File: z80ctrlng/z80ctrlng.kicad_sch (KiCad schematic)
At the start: 43 parts, among them J1 BUS, J2 Micro_SD_Card_Det2, J3 UEXT, J4 SERIAL, J5 Conn_01x04_Pin, Q4 BSS138, SW1 RESET, SW2 SW_DPDT_x2, SW3 SW_SP3T, SW4 SW_DIP_x06, SW5 SW_DPDT_x2, SW6 SW_DPDT_x2, U1 AVR128DB64x-xPT, U2 MIC5504-3.3YM5, U3 MCP7940N-xST, U5 74HCT574, U6 74HCT257, U7 AS6C4008-55PCN, Y1 32kHz

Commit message: Finishing up...
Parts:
- removed J5: Conn_01x04_Pin, Connector_PinHeader_2.54mm:PinHeader_1x04_P2.54mm_Horizontal, symbol Connector:Conn_01x04_Pin
- removed SW5, SW6: SW_DPDT_x2, SamacSys_Parts:JS202011CQN, symbol Switch:SW_DPDT_x2
- added C15: 0.1uf, Capacitor_SMD:C_0402_1005Metric, symbol Device:C_Small
- added D1: LED, LED_SMD:LED_0805_2012Metric, symbol Device:LED
- added J6: UPDI, Connector_PinHeader_2.54mm:PinHeader_1x04_P2.54mm_Horizontal, symbol Connector_Generic:Conn_01x04
- added R10: 330, Resistor_SMD:R_0402_1005Metric, symbol Device:R_Small
- added SW5, SW6: SW_DPST, SamacSys_Parts:JS202011CQN, symbol Switch:SW_DPST
- BT1: footprint Battery:BatteryHolder_Keystone_3000_1x12mm -> Battery:BatteryHolder_Keystone_3001_1x12mm
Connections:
- net +3.3V: now also D1.2 (A)
- net +5V: now also C15.1, J6.3 (Pin_3)
- net GND: now also C15.2, J6.2 (Pin_2)
- net SCL: now also SW6.2
- net SCL3V: now also SW6.1
- net SCL5V: now also SW5.1
- net SDA: now also SW6.5
- net SDA3V: now also SW6.4
- net SDA5V: now also SW5.4
- net USER6: now also SW5.2
- net USER7: now also SW5.5
- net ~{RESET}: now also J6.1 (Pin_1)
- net ~{SDCS}: now also R10.1
- net at J3.10 (Pin_10), SW3.2: now also SW3.5
- net UPDI: now reaches U1.51 (UPDI)
- net UPDI: now also J6.4 (Pin_4)
- new net: D1.1 (K), R10.2
- no-connect marks 14 -> 11
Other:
- company: (none) -> (C) 2023 J.B. Langston
- title: (none) -> z80ctrl NG
- moved on the sheet: R9, SW2B

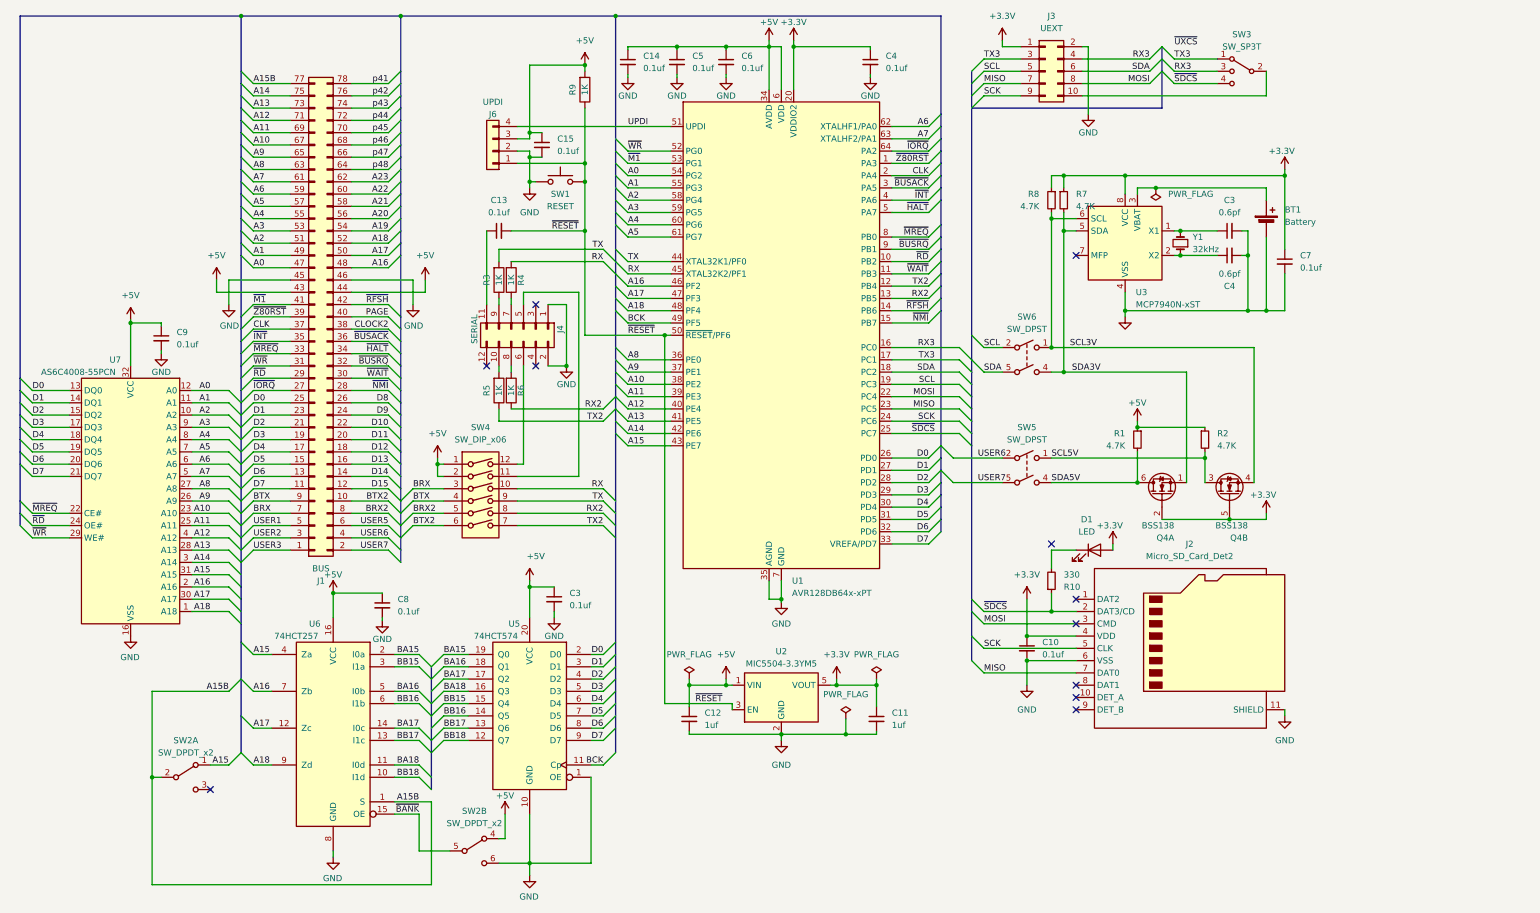
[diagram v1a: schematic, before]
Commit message: Rework bus links using jumpers instead of dip switches; add labels
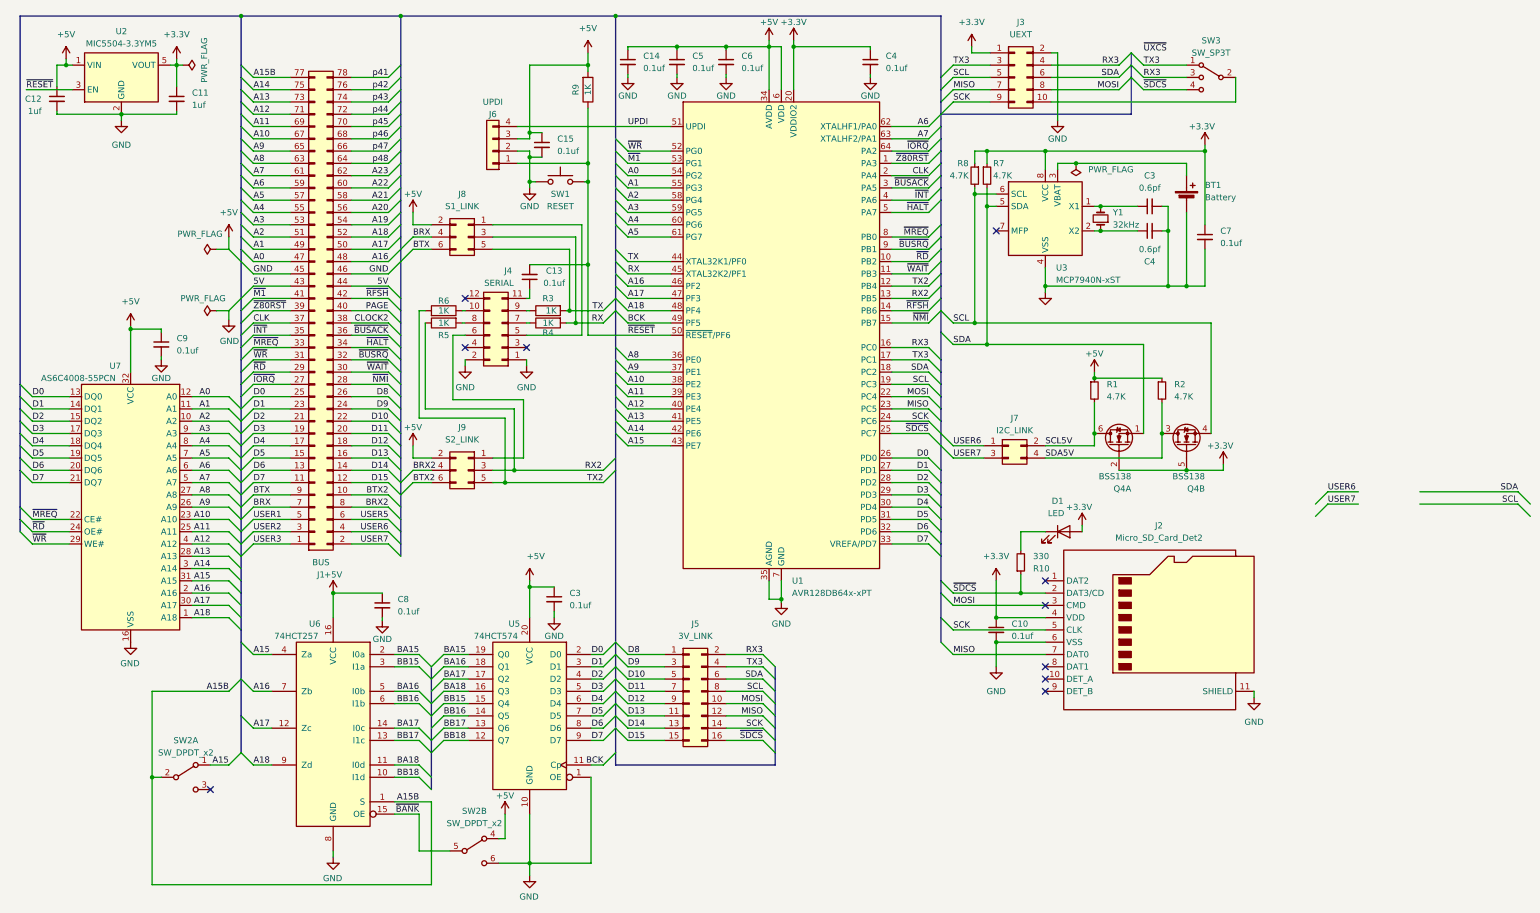
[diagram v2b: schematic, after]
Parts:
- removed SW4: SW_DIP_x06, Button_Switch_THT:SW_DIP_SPSTx06_Slide_9.78x17.42mm_W7.62mm_P2.54mm, symbol Switch:SW_DIP_x06
- removed SW5, SW6: SW_DPST, SamacSys_Parts:JS202011CQN, symbol Switch:SW_DPST
- added J5: 3V_LINK, Connector_PinHeader_2.54mm:PinHeader_2x08_P2.54mm_Vertical, symbol Connector_Generic:Conn_02x08_Odd_Even
- added J7: I2C_LINK, Connector_PinHeader_2.54mm:PinHeader_2x02_P2.54mm_Vertical, symbol Connector_Generic:Conn_02x02_Odd_Even
- added J8: S1_LINK, Connector_PinHeader_2.54mm:PinHeader_2x03_P2.54mm_Vertical, symbol Connector_Generic:Conn_02x03_Odd_Even
- added J9: S2_LINK, Connector_PinHeader_2.54mm:PinHeader_2x03_P2.54mm_Vertical, symbol Connector_Generic:Conn_02x03_Odd_Even
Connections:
- net SCL3V is gone; now on net SCL: Q4.4 (S), R8.2, U3.6 (SCL)
- net SDA3V is gone; now on net SDA: Q4.1 (S), R7.2, U3.5 (SDA)
- net +5V: now also J8.2 (Pin_2), J9.2 (Pin_2); no longer J1.43 (Pin_43), J1.44 (Pin_44)
- net BRX: now also J8.4 (Pin_4)
- net BRX2: now also J9.4 (Pin_4)
- net BTX: now also J8.6 (Pin_6)
- net BTX2: now also J9.6 (Pin_6)
- net D10: now also J5.5 (Pin_5)
- net D11: now also J5.7 (Pin_7)
- net D12: now also J5.9 (Pin_9)
- net D13: now also J5.11 (Pin_11)
- net D14: now also J5.13 (Pin_13)
- net D15: now also J5.15 (Pin_15)
- net D8: now also J5.1 (Pin_1)
- net D9: now also J5.3 (Pin_3)
- net MISO: now also J5.12 (Pin_12)
- net MOSI: now also J5.10 (Pin_10)
- net RX: now also J8.3 (Pin_3)
- net RX2: now also R5.1, J9.3 (Pin_3); no longer R6.1
- net RX3: now also J5.2 (Pin_2)
- net SCK: now also J5.14 (Pin_14)
- net SCL: now also J5.8 (Pin_8)
- net SCL5V: now also Q4.6 (D), R1.2, J7.2 (Pin_2); no longer Q4.3 (D), R2.2
- net SDA: now also J5.6 (Pin_6)
- net SDA5V: now also Q4.3 (D), R2.2, J7.4 (Pin_4); no longer Q4.6 (D), R1.2
- net TX: now also J8.5 (Pin_5)
- net TX2: now also R6.2, J9.5 (Pin_5); no longer R5.1
- net TX3: now also J5.4 (Pin_4)
- net USER6: now also J7.1 (Pin_1)
- net USER7: now also J7.3 (Pin_3)
- net ~{SDCS}: now also J5.16 (Pin_16)
- net at J4.10 (Pin_10): now also R6.1; no longer R5.2
- net at J4.5 (Pin_5): now also J8.1 (Pin_1)
- net at J4.6 (Pin_6): now also J9.1 (Pin_1)
- net at J4.8 (Pin_8): now also R5.2; no longer R6.2
- new net 5V: J1.43 (Pin_43), J1.44 (Pin_44)
- no-connect marks 11 -> 10
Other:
- moved on the sheet: BT1, C10, C11, C12, C13, C3, C4, C7, C9, D1, J1, J2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

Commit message: More cleanup, fixing errors
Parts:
- removed C4: 0.6pf, Capacitor_SMD:C_0402_1005Metric, symbol Device:C_Small
- removed C7: 0.1uf, Capacitor_SMD:C_0402_1005Metric, symbol Device:C_Small
- removed J7: I2C_LINK, Connector_PinHeader_2.54mm:PinHeader_2x02_P2.54mm_Vertical, symbol Connector_Generic:Conn_02x02_Odd_Even
- removed R7, R8: 4.7K, Resistor_SMD:R_0402_1005Metric, symbol Device:R_Small
- removed SW3: SW_SP3T, SamacSys_Parts:OS103011MS8QP1, symbol Switch:SW_SP3T
- removed U3: MCP7940N-xST, Package_SO:TSSOP-8_3x3mm_P0.65mm, symbol Timer_RTC:MCP7940N-xST
- added C1, C2: 0.6pf, Capacitor_SMD:C_0402_1005Metric, symbol Device:C_Small
- added J10: QWIIC, Custom:JST_SM04B-SRSS-TB_LF__SN_, symbol Connector_Generic:Conn_01x04
- added J7: UEXT_CS, Connector_PinHeader_2.54mm:PinHeader_2x05_P2.54mm_Vertical, symbol Connector_Generic:Conn_02x05_Odd_Even
- added R11, R12, R13, R14: 100K, Resistor_SMD:R_0402_1005Metric, symbol Device:R_Small
- added R3, R4: 4.7K, Resistor_SMD:R_0402_1005Metric, symbol Device:R_Small
- added SW1 (x2): RTC, Custom:SWITCH_011CQN, symbol Switch:SW_DPST
- added U1: MCP7940N-xST, Package_SO:TSSOP-8_3x3mm_P0.65mm, symbol Timer_RTC:MCP7940N-xST
- C3: value 0.6pf -> 0.1uf
- J2: value Micro_SD_Card_Det2 -> MICRO_SD
- SW2: value SW_DPDT_x2 -> BANK_EN; footprint SamacSys_Parts:JS202011CQN -> Custom:SWITCH_011CQN
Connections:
- net 5V is gone; now on net +5V: J1.43 (Pin_43), J1.44 (Pin_44)
- net +3.3V: now also C3.1, J10.3 (Pin_3), R11.1, R12.1, R13.1, R3.1, R4.1, U1.8 (VCC)
- net +5V: now also J6.2 (Pin_2), J8.1 (Pin_1), J9.1 (Pin_1), SW2.6 (C); no longer J6.3 (Pin_3), J8.2 (Pin_2), J9.2 (Pin_2), SW2.4 (A)
- net GND: now also J6.3 (Pin_3), SW2.4 (A), C1.2, C2.2, J10.4 (Pin_4), R14.1, U1.4 (VSS); no longer J6.2 (Pin_2), SW2.6 (C)
- net MISO: now also R11.2
- net MOSI: now also R13.2
- net RX3: now also J7.3 (Pin_3)
- net SCK: now also R14.2
- net SCL: now also J10.1 (Pin_1), J7.5 (Pin_5), R3.2, SW1.1
- net SCL5V: now also Q4.3 (D), R2.2, SW1.6; no longer Q4.6 (D), R1.2
- net SDA: now also J10.2 (Pin_2), J7.7 (Pin_7), R4.2, SW1.2
- net SDA5V: now also Q4.6 (D), R1.2, SW1.5; no longer Q4.3 (D), R2.2
- net TX3: now also J7.1 (Pin_1)
- net USER6: now also SW1.1
- net USER7: now also SW1.2
- net ~{SDCS}: now also J7.9 (Pin_9), R12.2
- net ~{UXCS}: now also J3.10 (Pin_10), J7.10 (Pin_10), J7.2 (Pin_2), J7.4 (Pin_4), J7.6 (Pin_6), J7.8 (Pin_8)
- net 5VS2: now reaches J4.6 (Pin_6)
- net 5VS2: now also J9.2 (Pin_2); no longer J9.1 (Pin_1)
- net at Y1.2: now also C1.1, U1.1 (X1); no longer C3.1
- net at Y1.1: now also C2.1, U1.2 (X2)
- net at BT1.1 (+): now also U1.3 (VBAT)
- net 5VS1: now reaches J4.5 (Pin_5)
- net 5VS1: now also J8.2 (Pin_2); no longer J8.1 (Pin_1)
- net CLK renamed Z80CLK
- new net: SW1.5, U1.5 (SDA)
- new net: SW1.6, U1.6 (SCL)
- no-connect marks 10 -> 9
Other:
- moved on the sheet: C10, C11, C12, C13, C15, D1, J2, J3, J4, J5, J6, J8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

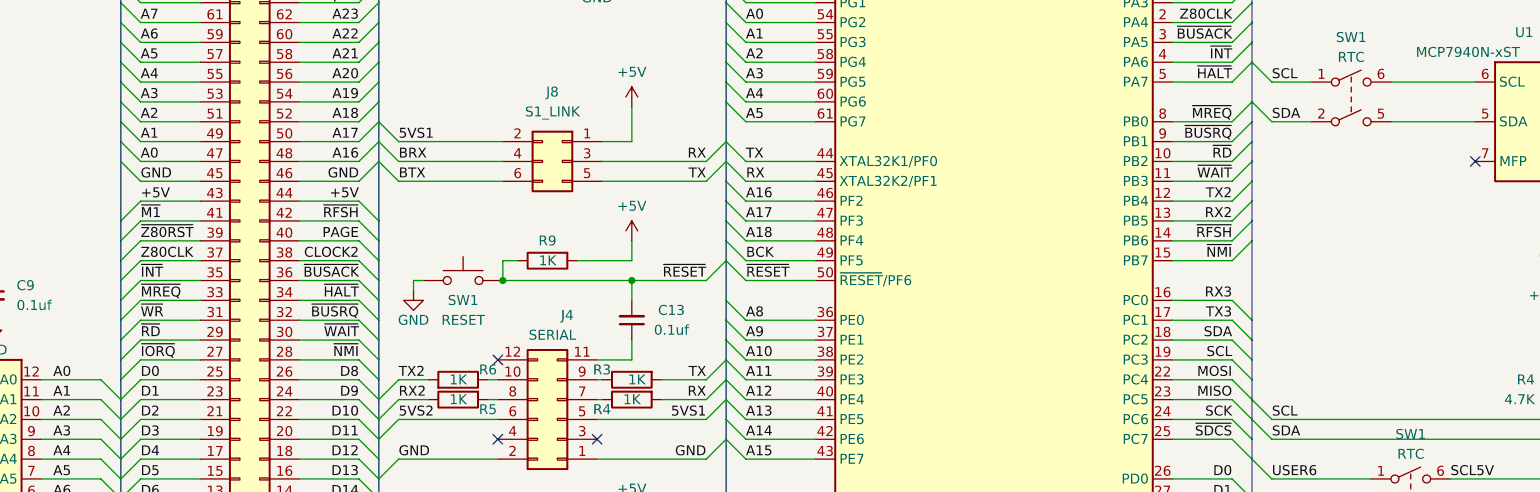
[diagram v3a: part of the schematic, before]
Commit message: Rework to make room for clock jumper
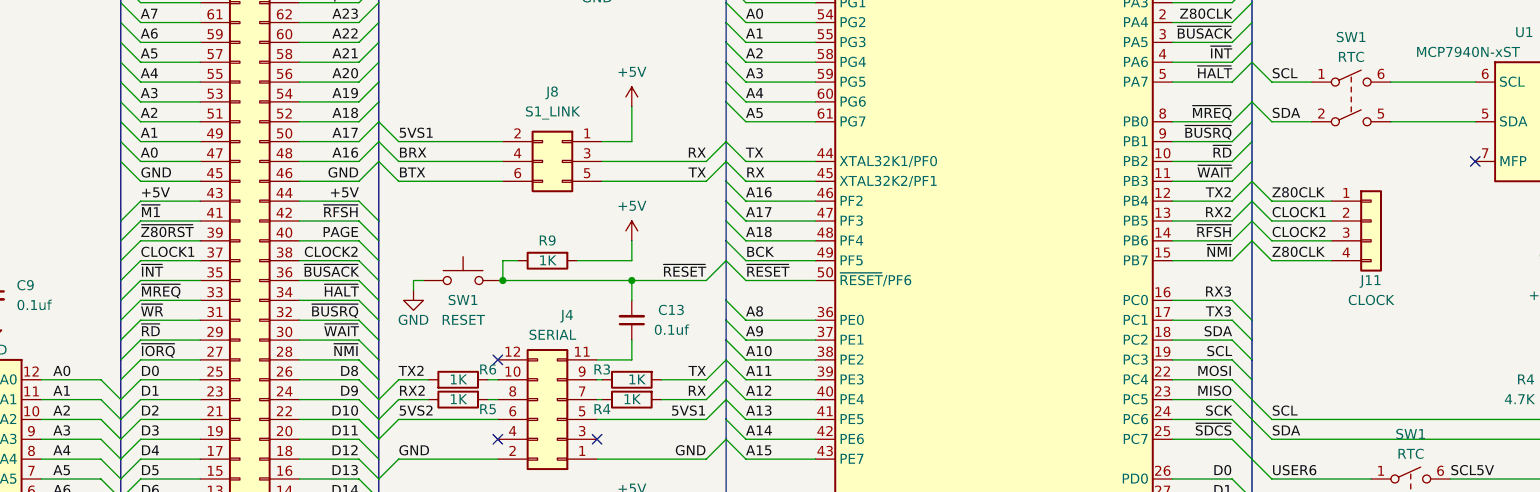
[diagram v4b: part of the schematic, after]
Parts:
- added J11: CLOCK, Connector_PinHeader_2.54mm:PinHeader_1x04_P2.54mm_Vertical, symbol Connector_Generic:Conn_01x04
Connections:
- net CLOCK2: now also J11.3 (Pin_3)
- net Z80CLK: now also J11.1 (Pin_1), J11.4 (Pin_4); no longer J1.37 (Pin_37)
- new net CLOCK1: J1.37 (Pin_37), J11.2 (Pin_2)
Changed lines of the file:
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@@
     (stroke (width 0) (type default))
   )
+  (bus_entry (at 207.01 74.93) (size -2.54 -2.54)
+    (stroke (width 0) (type default))
+  )
   (bus_entry (at 59.69 125.73) (size 2.54 -2.54)
     (stroke (width 0) (type default))
@@
     (stroke (width 0) (type default))
   )
+  (bus_entry (at 207.01 69.85) (size -2.54 -2.54)
+    (stroke (width 0) (type default))
+  )
   (bus_entry (at 237.49 26.67) (size 2.54 2.54)
     (stroke (width 0) (type default))
@@
     (stroke (width 0) (type default))
   )
+  (bus_entry (at 207.01 77.47) (size -2.54 -2.54)
+    (stroke (width 0) (type default))
+  )
   (bus_entry (at 201.93 59.69) (size 2.54 -2.54)
     (stroke (width 0) (type default))
@@
     (stroke (width 0) (type default))
   )
+  (bus_entry (at 207.01 72.39) (size -2.54 -2.54)
+    (stroke (width 0) (type default))
+  )
   (bus_entry (at 201.93 72.39) (size 2.54 -2.54)
     (stroke (width 0) (type default))
@@
     (stroke (width 0) (type default))
   )
+  (wire (pts (xy 207.01 69.85) (xy 214.63 69.85))
+    (stroke (width 0) (type default))
+  )
   (wire (pts (xy 139.7 46.99) (xy 148.59 46.99))
     (stroke (width 0) (type default))
@@
     (stroke (width 0) (type default))
   )
+  (wire (pts (xy 207.01 72.39) (xy 214.63 72.39))
+    (stroke (width 0) (type default))
+  )
   (wire (pts (xy 278.765 115.57) (xy 276.225 115.57))
     (stroke (width 0) (type default))
@@
     (stroke (width 0) (type default))
   )
+  (wire (pts (xy 207.01 77.47) (xy 214.63 77.47))
+    (stroke (width 0) (type default))
+  )
   (wire (pts (xy 139.7 54.61) (xy 148.59 54.61))
     (stroke (width 0) (type default))
@@
     (stroke (width 0) (type default))
   )
+  (wire (pts (xy 207.01 74.93) (xy 214.63 74.93))
+    (stroke (width 0) (type default))
+  )
   (bus (pts (xy 137.16 39.37) (xy 137.16 41.91))
     (stroke (width 0) (type default))
@@
     (effects (font (size 1.27 1.27)) (justify right bottom))
   )
+  (label "CLOCK2" (at 207.01 74.93 0) (fields_autoplaced)
+    (effects (font (size 1.27 1.27)) (justify left bottom))
+  )
   (label "~{INT}" (at 62.23 80.01 0) (fields_autoplaced)
     (effects (font (size 1.27 1.27)) (justify left bottom))
@@
     (effects (font (size 1.27 1.27)) (justify left bottom))
   )
-  (label "Z80CLK" (at 62.23 77.47 0) (fields_autoplaced)
+  (label "CLOCK1" (at 62.23 77.47 0) (fields_autoplaced)
     (effects (font (size 1.27 1.27)) (justify left bottom))
   )
@@
     (effects (font (size 1.27 1.27)) (justify left bottom))
   )
+  (label "CLOCK1" (at 207.01 72.39 0) (fields_autoplaced)
+    (effects (font (size 1.27 1.27)) (justify left bottom))
+  )
   (label "~{MREQ}" (at 16.51 118.11 0) (fields_autoplaced)
     (effects (font (size 1.27 1.27)) (justify left bottom))
@@
     (effects (font (size 1.27 1.27)) (justify left bottom))
   )
+  (label "Z80CLK" (at 207.01 77.47 0) (fields_autoplaced)
+    (effects (font (size 1.27 1.27)) (justify left bottom))
+  )
   (label "RX" (at 139.7 67.31 0) (fields_autoplaced)
     (effects (font (size 1.27 1.27)) (justify left bottom))
@@
     (effects (font (size 1.27 1.27)) (justify right bottom))
   )
+  (label "Z80CLK" (at 207.01 69.85 0) (fields_autoplaced)
+    (effects (font (size 1.27 1.27)) (justify left bottom))
+  )
   (label "SCK" (at 207.01 34.29 0) (fields_autoplaced)
     (effects (font (size 1.27 1.27)) (justify left bottom))
@@
     (effects (font (size 1.27 1.27)) (justify right bottom))
   )
+  (symbol (lib_id "Connector_Generic:Conn_01x04") (at 219.71 72.39 0) (unit 1)
+    (in_bom yes) (on_board yes) (dnp no)
+    (property "Reference" "J11" (at 219.71 80.01 0)
+      (effects (font (size 1.27 1.27)))
+    )
+    (property "Value" "CLOCK" (at 219.71 82.55 0)
+      (effects (font (size 1.27 1.27)))
+    )
+    (property "Footprint" "Connector_PinHeader_2.54mm:PinHeader_1x04_P2.54mm_Vertical" (at 219.71 72.39 0)
+      (effects (font (size 1.27 1.27)) hide)
+    )
+    (property "Datasheet" "~" (at 219.71 72.39 0)
+      (effects (font (size 1.27 1.27)) hide)
+    )
+    (pin "1")
+    (pin "2")
+    (pin "3")
+    (pin "4")
+    (instances
+      (project "z80ctrlng"
+        (path "/9c261024-c69f-48e3-a573-d08c538d0e71"
+          (reference "J11") (unit 1)
+        )
+      )
+    )
+  )
   (symbol (lib_id "Device:C_Small") (at 189.865 23.495 0) (unit 1)
